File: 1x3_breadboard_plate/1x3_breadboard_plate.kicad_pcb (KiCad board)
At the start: 2 copper layers, 72.2 x 22 mm, 4 parts

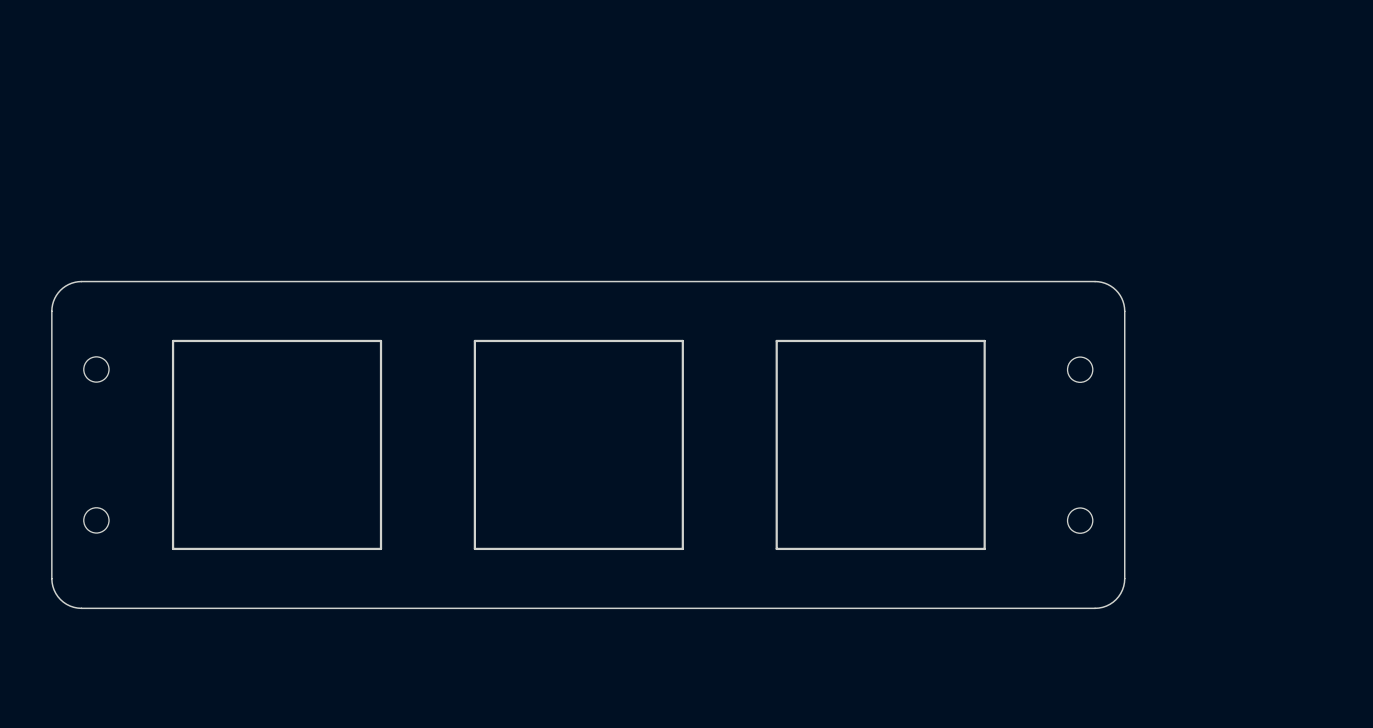
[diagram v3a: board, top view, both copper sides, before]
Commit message: converts to 19.05x19.05mm
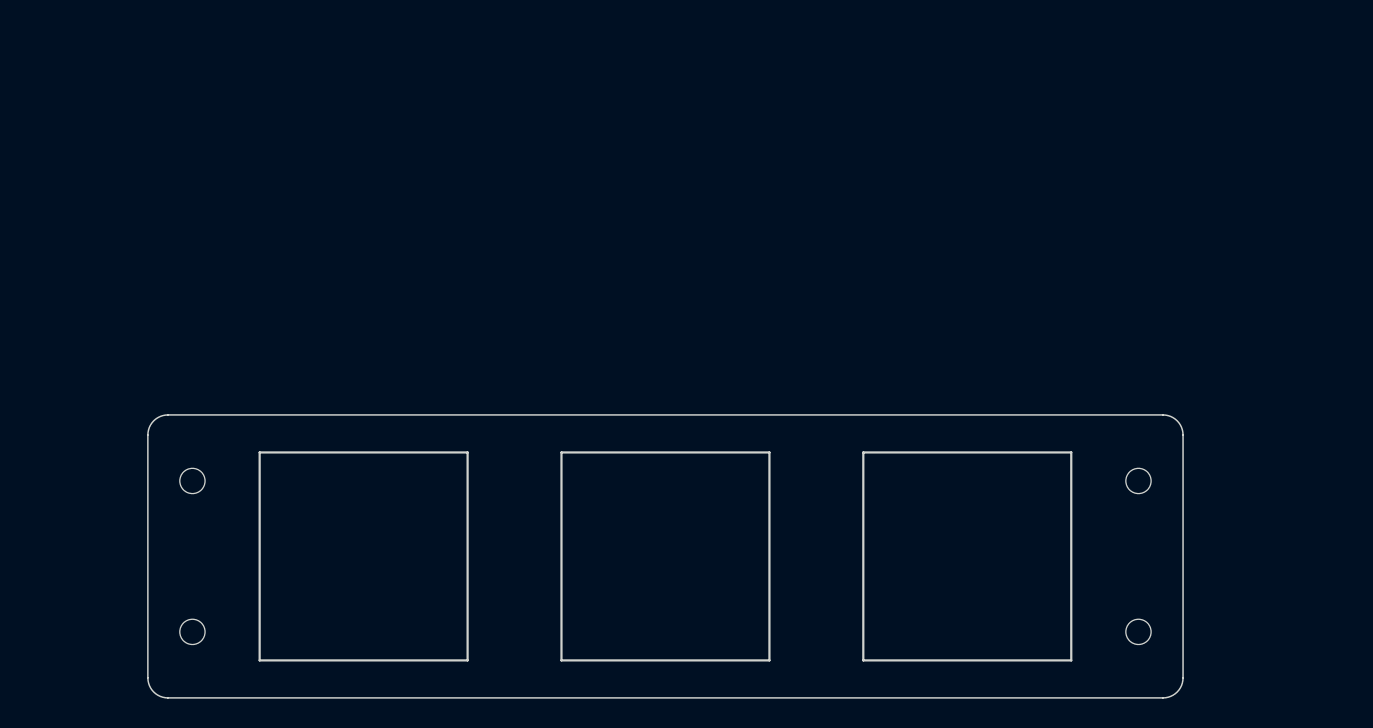
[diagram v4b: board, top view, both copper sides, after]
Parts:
- moved H1 9.91 mm to (100.2, 100.3)
- moved H2 9.91 mm to (100.2, 110.5)
- moved H3 8.46 mm to (163.9, 100.3)
- moved H4 8.46 mm to (163.9, 110.5)
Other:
- board size 72.2 x 22 mm -> 69.7 x 19 mm
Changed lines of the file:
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@@
   (net 0 "")
   (footprint "PCM_kikit:NPTH" (layer "F.Cu")
-    (at 160 103)
-    (attr through_hole)
-    (fp_text reference "H4" (at 0 0.5) (layer "F.SilkS") hide
-        (effects (font (size 1 1) (thickness 0.15)))
-    )
-    (fp_text value "NPTH" (at 0 -0.5) (layer "F.Fab") hide
-        (effects (font (size 1 1) (thickness 0.15)))
-    )
-    (pad "" np_thru_hole circle (at 0 0) (size 1.7 1.7) (drill 1.7) (layers "*.Mask"))
-  )
-  (footprint "PCM_kikit:NPTH" (layer "F.Cu")
-    (at 93.77 92.825)
+    (at 100.235 100.33)
     (attr through_hole)
     (fp_text reference "H1" (at 0 0.5) (layer "F.SilkS") hide
@@
   )
   (footprint "PCM_kikit:NPTH" (layer "F.Cu")
-    (at 93.77 102.985)
+    (at 100.235 110.49)
     (attr through_hole)
     (fp_text reference "H2" (at 0 0.5) (layer "F.SilkS") hide
@@
   )
   (footprint "PCM_kikit:NPTH" (layer "F.Cu")
-    (at 160 92.84)
+    (at 163.925 100.33)
     (attr through_hole)
     (fp_text reference "H3" (at 0 0.5) (layer "F.SilkS") hide
@@
     (pad "" np_thru_hole circle (at 0 0) (size 1.7 1.7) (drill 1.7) (layers "*.Mask"))
   )
-  (gr_arc (start 129.540026 124.705) (mid 127.54 122.705) (end 129.540026 120.705)
-    (stroke (width 0.15) (type default)) (layer "Dwgs.User"))
-  (gr_arc (start 110.48997 120.705) (mid 112.49 122.705) (end 110.48997 124.705)
-    (stroke (width 0.15) (type default)) (layer "Dwgs.User"))
-  (gr_arc (start 90.77 88.905) (mid 91.355784 87.490775) (end 92.77 86.905)
+  (footprint "PCM_kikit:NPTH" (layer "F.Cu")
+    (at 163.925 110.49)
+    (attr through_hole)
+    (fp_text reference "H4" (at 0 0.5) (layer "F.SilkS") hide
+        (effects (font (size 1 1) (thickness 0.15)))
+    )
+    (fp_text value "NPTH" (at 0 -0.5) (layer "F.Fab") hide
+        (effects (font (size 1 1) (thickness 0.15)))
+    )
+    (pad "" np_thru_hole circle (at 0 0) (size 1.7 1.7) (drill 1.7) (layers "*.Mask"))
+  )
+  (gr_rect (start 145.4 98.41) (end 159.4 112.41)
+    (stroke (width 0.15) (type default)) (fill none) (layer "Edge.Cuts"))
+  (gr_rect (start 125.08 98.41) (end 139.08 112.41)
+    (stroke (width 0.15) (type default)) (fill none) (layer "Edge.Cuts"))
+  (gr_line (start 166.925 97.235) (end 166.925 113.585)
     (stroke (width 0.1) (type default)) (layer "Edge.Cuts"))
-  (gr_rect (start 139.57 90.905) (end 153.57 104.905)
+  (gr_arc (start 166.925 113.585) (mid 166.529594 114.539594) (end 165.575 114.935)
+    (stroke (width 0.1) (type default)) (layer "Edge.Cuts"))
+  (gr_arc (start 165.575 95.885) (mid 166.529594 96.280406) (end 166.925 97.235)
+    (stroke (width 0.1) (type default)) (layer "Edge.Cuts"))
+  (gr_arc (start 98.585 114.935) (mid 97.630407 114.539594) (end 97.235 113.585)
+    (stroke (width 0.1) (type default)) (layer "Edge.Cuts"))
+  (gr_arc (start 97.235 97.235) (mid 97.630406 96.280406) (end 98.585 95.885)
+    (stroke (width 0.1) (type default)) (layer "Edge.Cuts"))
+  (gr_line (start 165.575 114.935) (end 98.585 114.935)
+    (stroke (width 0.1) (type default)) (layer "Edge.Cuts"))
+  (gr_line (start 165.575 95.885) (end 98.585 95.885)
+    (stroke (width 0.1) (type default)) (layer "Edge.Cuts"))
+  (gr_line (start 97.235 113.585) (end 97.235 97.235)
+    (stroke (width 0.1) (type default)) (layer "Edge.Cuts"))
+  (gr_rect (start 104.76 98.41) (end 118.76 112.41)
     (stroke (width 0.15) (type default)) (fill none) (layer "Edge.Cuts"))
-  (gr_arc (start 161 86.905) (mid 162.414235 87.490775) (end 163 88.905)
-    (stroke (width 0.1) (type default)) (layer "Edge.Cuts"))
-  (gr_arc (start 92.77 108.905) (mid 91.355808 108.319202) (end 90.77 106.905)
-    (stroke (width 0.1) (type default)) (layer "Edge.Cuts"))
-  (gr_rect (start 119.25 90.905) (end 133.25 104.905)
-    (stroke (width 0.15) (type default)) (fill none) (layer "Edge.Cuts"))
-  (gr_line (start 163 88.905) (end 163 106.905)
-    (stroke (width 0.1) (type default)) (layer "Edge.Cuts"))
-  (gr_line (start 161 108.905) (end 92.77 108.905)
-    (stroke (width 0.1) (type default)) (layer "Edge.Cuts"))
-  (gr_line (start 161 86.905) (end 92.77 86.905)
-    (stroke (width 0.1) (type default)) (layer "Edge.Cuts"))
-  (gr_line (start 90.77 106.905) (end 90.77 88.905)
-    (stroke (width 0.1) (type default)) (layer "Edge.Cuts"))
-  (gr_rect (start 98.93 90.905) (end 112.93 104.905)
-    (stroke (width 0.15) (type default)) (fill none) (layer "Edge.Cuts"))
-  (gr_arc (start 163 106.905) (mid 162.414212 108.319202) (end 161 108.905)
-    (stroke (width 0.1) (type default)) (layer "Edge.Cuts"))
-  (gr_rect (start 140.995 81.94) (end 159.995 100.94)
-    (stroke (width 0.15) (type default)) (fill none) (layer "Margin"))
-  (gr_rect (start 120.675 81.94) (end 139.675 100.94)
-    (stroke (width 0.15) (type default)) (fill none) (layer "Margin"))
-  (gr_rect (start 100.355 81.94) (end 119.355 100.94)
-    (stroke (width 0.15) (type default)) (fill none) (layer "Margin"))
   (zone (net 0) (net_name "") (layers "*.Mask") (hatch edge 0.5)
     (connect_pads (clearance 0.5))
@@
     (polygon
       (pts
-        (xy 90 86)
-        (xy 164 86)
-        (xy 164 110)
-        (xy 90 110)
+        (xy 95.83 94.775)
+        (xy 168.56 94.775)
+        (xy 168.56 116.235)
+        (xy 95.83 116.235)
       )
     )
